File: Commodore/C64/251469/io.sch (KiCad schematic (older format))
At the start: 25 parts, among them CN4 Serial Bus, CN8 Control Port 2, CN9 Control Port 1, U1 6526, U2 6526, U27 74LS08, U28 4066, U8 7406

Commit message: refac: extracted serial bus to separate sheet
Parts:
- removed CN4: Serial Bus, symbol Connector:DIN-6
- added unit 1 of RP3
- added unit 2 of RP3
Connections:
- net labels removed: ATN, CLK, DATA, SRQ, ~EXTRST
- wire segments 194 -> 201
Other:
- note added: "CASS RD\nSRQ IN"
- note removed: "CASS RD"
- moved on the sheet: CR100, CR101, CR102, CR103
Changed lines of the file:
@@
 $Descr A4 11693 8268
 encoding utf-8
-Sheet 8 10
-Title "Commodore 64 - I/O section (schematic #251469)"
+Sheet 8 11
+Title "Commodore 64 - I/O Section (schematic #251469)"
 Date "2019-07-15"
 Rev "0.1"
@@
 Wire Wire Line
 	2700 4150 2950 4150
-Text HLabel 2700 7150 3    50   Output ~ 0
+Text HLabel 2700 7400 3    50   Output ~ 0
 ~IRQ
-Text HLabel 5600 7150 3    50   Output ~ 0
+Text HLabel 5600 7400 3    50   Output ~ 0
 ~NMI
-$Comp
-L Connector:DIN-6 CN4
-U 1 1 5D647908
-P 9500 3950
-F 0 "CN4" H 8600 4350 50  0000 C CNN
-F 1 "Serial Bus" H 8750 4250 50  0000 C CNN
-F 2 "" H 9500 3950 50  0001 C CNN
-F 3 "http://www.mouser.com/ds/2/18/40_c091_abd_e-75918.pdf" H 9500 3950 50  0001 C CNN
-	1    9500 3950
-	-1   0    0    -1
-$EndComp
-Wire Wire Line
-	10000 3900 10000 3850
-Text HLabel 9650 4300 2    50   Input ~ 0
-~EXTRST
-$Comp
-L power:GND #PWR?
-U 1 1 5D64C58B
-P 10000 3900
-F 0 "#PWR?" H 10000 3650 50  0001 C CNN
-F 1 "GND" H 10005 3727 50  0000 C CNN
-F 2 "" H 10000 3900 50  0001 C CNN
-F 3 "" H 10000 3900 50  0001 C CNN
-	1    10000 3900
-	-1   0    0    -1
-$EndComp
-Wire Wire Line
-	9500 4250 9500 4300
-Wire Wire Line
-	9500 4300 9650 4300
-Wire Wire Line
-	9200 4050 7850 4050
-Wire Wire Line
-	9200 3850 7850 3850
-Text Label 9200 4050 2    50   ~ 0
-DATA
-Text Label 9200 3850 2    50   ~ 0
-CLK
-Wire Wire Line
-	9500 3650 7850 3650
-Wire Wire Line
-	9800 3850 10000 3850
-Text Label 9500 3650 2    50   ~ 0
-ATN
-Wire Wire Line
-	9800 4050 9850 4050
-Wire Wire Line
-	9850 4050 9850 3550
-Wire Wire Line
-	9850 3550 7850 3550
-Text Label 9850 3550 2    50   ~ 0
-SRQ
-$Comp
-L Device:D CR100
-U 1 1 5D6E038A
-P -3300 4150
-F 0 "CR100" H -3300 4366 50  0000 C CNN
-F 1 "1N4148" H -3300 4275 50  0000 C CNN
-F 2 "" H -3300 4150 50  0001 C CNN
-F 3 "~" H -3300 4150 50  0001 C CNN
-	1    -3300 4150
-	1    0    0    -1
-$EndComp
 $Comp
 L Device:D CR101
 U 1 1 5D6E1332
-P -3300 4500
-F 0 "CR101" H -3300 4716 50  0000 C CNN
-F 1 "1N4148" H -3300 4625 50  0000 C CNN
-F 2 "" H -3300 4500 50  0001 C CNN
-F 3 "~" H -3300 4500 50  0001 C CNN
-	1    -3300 4500
-	1    0    0    -1
-$EndComp
-$Comp
-L Device:D CR102
-U 1 1 5D6E3186
-P -2750 4150
-F 0 "CR102" H -2750 4366 50  0000 C CNN
-F 1 "1N4148" H -2750 4275 50  0000 C CNN
-F 2 "" H -2750 4150 50  0001 C CNN
-F 3 "~" H -2750 4150 50  0001 C CNN
-	1    -2750 4150
-	1    0    0    -1
+P 8150 4450
+F 0 "CR101" H 8150 4666 50  0000 C CNN
+F 1 "1N4148" H 8150 4575 50  0000 C CNN
+F 2 "" H 8150 4450 50  0001 C CNN
+F 3 "~" H 8150 4450 50  0001 C CNN
+	1    8150 4450
+	0    1    1    0
 $EndComp
 $Comp
 L Device:D CR103
 U 1 1 5D6E318C
-P -2750 4500
-F 0 "CR103" H -2750 4716 50  0000 C CNN
-F 1 "1N4148" H -2750 4625 50  0000 C CNN
-F 2 "" H -2750 4500 50  0001 C CNN
-F 3 "~" H -2750 4500 50  0001 C CNN
-	1    -2750 4500
-	1    0    0    -1
+P 7800 4450
+F 0 "CR103" H 7800 4666 50  0000 C CNN
+F 1 "1N4148" H 7800 4575 50  0000 C CNN
+F 2 "" H 7800 4450 50  0001 C CNN
+F 3 "~" H 7800 4450 50  0001 C CNN
+	1    7800 4450
+	0    1    1    0
 $EndComp
 $Comp
@@
 $EndComp
 Text Notes 1550 5350 0    50   ~ 0
-CASS RD
+CASS RD\nSRQ IN
 Text Notes 5650 3450 0    50   ~ 0
 ~VA14
@@
 COL[0..7]
 Wire Wire Line
-	2700 5350 2700 7150
+	2700 5350 2700 7400
 Wire Wire Line
 	5600 5350 5600 6400
@@
 Wire Wire Line
 	4500 6400 5600 6400
-Connection ~ 5600 6400
-Wire Wire Line
-	5600 6400 5600 7150
+Wire Wire Line
+	5600 6400 5600 7250
 Wire Wire Line
 	6500 5850 6500 6200
@@
 	7150 3500 7600 3500
 Wire Wire Line
-	7300 3850 7600 3850
-Wire Wire Line
 	7050 4200 7450 4200
 Wire Wire Line
 	7450 3450 7450 4200
 Connection ~ 7450 4200
-Wire Wire Line
-	7450 4200 7600 4200
 Wire Wire Line
 	7150 3150 7150 3100
@@
 Wire Wire Line
 	7450 4600 7450 4200
+Wire Wire Line
+	7600 3500 7600 2700
+Wire Wire Line
+	7450 4200 8150 4200
+Wire Wire Line
+	8150 4200 8150 4300
+Connection ~ 7800 3850
+Wire Wire Line
+	7800 3850 7800 4300
+Wire Wire Line
+	7300 3850 7800 3850
+Connection ~ 8150 4200
+Wire Wire Line
+	7800 3850 7800 3450
+$Comp
+L Device:D CR102
+U 1 1 5D6E3186
+P 7800 3300
+F 0 "CR102" H 7800 3200 50  0000 C CNN
+F 1 "1N4148" H 7800 3425 50  0000 C CNN
+F 2 "" H 7800 3300 50  0001 C CNN
+F 3 "~" H 7800 3300 50  0001 C CNN
+	1    7800 3300
+	0    1    1    0
+$EndComp
+Wire Wire Line
+	7800 3150 7800 3100
+Wire Wire Line
+	7850 3100 8150 3100
+Connection ~ 7850 3100
+Wire Wire Line
+	7850 3050 7850 3100
+$Comp
+L power:+5V #PWR?
+U 1 1 5DD390BE
+P 7850 3050
+AR Path="/5DD390BE" Ref="#PWR?"  Part="1"
+AR Path="/5D28EBAC/5DD390BE" Ref="#PWR?"  Part="1"
+AR Path="/5D4AE438/5DD390BE" Ref="#PWR?"  Part="1"
+AR Path="/5D943305/5DD390BE" Ref="#PWR?"  Part="1"
+AR Path="/5D943305/5D47A471/5DD390BE" Ref="#PWR?"  Part="1"
+F 0 "#PWR?" H 7850 2900 50  0001 C CNN
+F 1 "+5V" H 7750 3200 50  0000 L CNN
+F 2 "" H 7850 3050 50  0001 C CNN
+F 3 "" H 7850 3050 50  0001 C CNN
+	1    7850 3050
+	1    0    0    -1
+$EndComp
+Wire Wire Line
+	8150 3100 8150 3150
+Wire Wire Line
+	7800 3100 7850 3100
+Wire Wire Line
+	8150 4200 8150 3450
+$Comp
+L Device:D CR100
+U 1 1 5D6E038A
+P 8150 3300
+F 0 "CR100" H 8150 3200 50  0000 C CNN
+F 1 "1N4148" H 8150 3425 50  0000 C CNN
+F 2 "" H 8150 3300 50  0001 C CNN
+F 3 "~" H 8150 3300 50  0001 C CNN
+	1    8150 3300
+	0    1    1    0
+$EndComp
+Wire Wire Line
+	7800 3850 8550 3850
+Wire Wire Line
+	8150 4200 8550 4200
+Wire Wire Line
+	7600 3500 8550 3500
+Connection ~ 7600 3500
+$Sheet
+S 9300 5050 750  350
+U 5DDE0343
+F0 "Serial Bus" 50
+F1 "serialbus.sch" 50
+$EndSheet
+$Comp
+L C64B:R_Network07_Split RP3
+U 1 1 5DE0B263
+P 4600 5100
+AR Path="/5D943305/5DE0B263" Ref="RP3"  Part="1"
+AR Path="/5D943305/5D47A471/5DE0B263" Ref="RP?"  Part="7"
+F 0 "RP3" V 4700 5000 50  0000 L CNN
+F 1 "3k3" V 4600 5050 25  0000 L CNN
+F 2 "" H 4700 5100 50  0001 C CNN
+F 3 "" H 4700 5100 50  0001 C CNN
+	1    4600 5100
+	1    0    0    -1
+$EndComp
+Connection ~ 4600 5350
+Wire Wire Line
+	4600 5350 4600 5300
+$Comp
+L power:+5V #PWR?
+U 1 1 5DE2E5EA
+P 4600 4850
+AR Path="/5DE2E5EA" Ref="#PWR?"  Part="1"
+AR Path="/5D28EBAC/5DE2E5EA" Ref="#PWR?"  Part="1"
+AR Path="/5D4AE438/5DE2E5EA" Ref="#PWR?"  Part="1"
+AR Path="/5D943305/5DE2E5EA" Ref="#PWR?"  Part="1"
+AR Path="/5D943305/5D47A471/5DE2E5EA" Ref="#PWR?"  Part="1"
+F 0 "#PWR?" H 4600 4700 50  0001 C CNN
+F 1 "+5V" H 4500 5000 50  0000 L CNN
+F 2 "" H 4600 4850 50  0001 C CNN
+F 3 "" H 4600 4850 50  0001 C CNN
+	1    4600 4850
+	1    0    0    -1
+$EndComp
+Wire Wire Line
+	4600 4850 4600 4900
+$Comp
+L C64B:R_Network07_Split RP3
+U 2 1 5DE3ABE8
+P 5800 7250
+AR Path="/5D943305/5DE3ABE8" Ref="RP3"  Part="2"
+AR Path="/5D943305/5D47A471/5DE3ABE8" Ref="RP?"  Part="7"
+F 0 "RP3" V 5900 7150 50  0000 L CNN
+F 1 "3k3" V 5800 7200 25  0000 L CNN
+F 2 "" H 5900 7250 50  0001 C CNN
+F 3 "" H 5900 7250 50  0001 C CNN
+	2    5800 7250
+	0    1    1    0
+$EndComp
+Connection ~ 5600 7250
+Wire Wire Line
+	5600 7250 5600 7400
+$Comp
+L power:+5V #PWR?
+U 1 1 5DE69A12
+P 6000 7200
+AR Path="/5DE69A12" Ref="#PWR?"  Part="1"
+AR Path="/5D28EBAC/5DE69A12" Ref="#PWR?"  Part="1"
+AR Path="/5D4AE438/5DE69A12" Ref="#PWR?"  Part="1"
+AR Path="/5D943305/5DE69A12" Ref="#PWR?"  Part="1"
+AR Path="/5D943305/5D47A471/5DE69A12" Ref="#PWR?"  Part="1"
+F 0 "#PWR?" H 6000 7050 50  0001 C CNN
+F 1 "+5V" H 5900 7350 50  0000 L CNN
+F 2 "" H 6000 7200 50  0001 C CNN
+F 3 "" H 6000 7200 50  0001 C CNN
+	1    6000 7200
+	1    0    0    -1
+$EndComp
+Connection ~ 5600 6400
+Wire Wire Line
+	6000 7250 6000 7200
 Wire Bus Line
 	4500 1100 4500 2750

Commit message: wip
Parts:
- added unit 3 of RP3
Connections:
- net labels added: ~EXTRST
- wire segments 201 -> 225
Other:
- moved on the sheet: C200, CR1, CR104, CR105, R100, R37, R5, U27C

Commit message: Using extracted R_Network07_Split from new Resistor_Pack library instead of embedding it in C64B library
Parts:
- removed RP3: 3k3, symbol C64B:R_Network07_Split
- added RP3: 3k3, symbol Resistor_Pack:R_Network07_Split
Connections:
- wire segments 225 -> 227
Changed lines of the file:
@@
 	4450 4250 4500 4250
 Wire Wire Line
-	4500 4250 4500 6500
-Wire Wire Line
 	4500 6500 5600 6500
-Wire Wire Line
-	5600 6500 5600 7350
 Wire Wire Line
 	7100 5850 7100 6200
@@
 	1    0    0    -1
 $EndComp
-$Comp
-L C64B:R_Network07_Split RP3
-U 4 1 5D94F7D8
-P 3950 6050
-AR Path="/5D943305/5D94F7D8" Ref="RP3"  Part="4"
-AR Path="/5D943305/5D47A471/5D94F7D8" Ref="RP?"  Part="4"
-F 0 "RP3" V 3950 6375 50  0000 L CNN
-F 1 "3k3" V 3950 6000 25  0000 L CNN
-F 2 "" H 4050 6050 50  0001 C CNN
-F 3 "" H 4050 6050 50  0001 C CNN
-	4    3950 6050
-	0    1    1    0
-$EndComp
-$Comp
-L C64B:R_Network07_Split RP3
-U 5 1 5D94F7DE
-P 3950 5950
-AR Path="/5D943305/5D94F7DE" Ref="RP3"  Part="5"
-AR Path="/5D943305/5D47A471/5D94F7DE" Ref="RP?"  Part="5"
-F 0 "RP3" V 3950 6275 50  0000 L CNN
-F 1 "3k3" V 3950 5900 25  0000 L CNN
-F 2 "" H 4050 5950 50  0001 C CNN
-F 3 "" H 4050 5950 50  0001 C CNN
-	5    3950 5950
-	0    1    1    0
-$EndComp
-$Comp
-L C64B:R_Network07_Split RP3
-U 6 1 5D94F7E4
-P 3950 5850
-AR Path="/5D943305/5D94F7E4" Ref="RP3"  Part="6"
-AR Path="/5D943305/5D47A471/5D94F7E4" Ref="RP?"  Part="6"
-F 0 "RP3" V 3950 6175 50  0000 L CNN
-F 1 "3k3" V 3950 5800 25  0000 L CNN
-F 2 "" H 4050 5850 50  0001 C CNN
-F 3 "" H 4050 5850 50  0001 C CNN
-	6    3950 5850
-	0    1    1    0
-$EndComp
 Wire Wire Line
 	3750 5750 3550 5750
@@
 Wire Wire Line
 	3750 6050 3250 6050
-$Comp
-L C64B:R_Network07_Split RP3
-U 7 1 5D94F7EA
-P 3950 5750
-AR Path="/5D943305/5D94F7EA" Ref="RP3"  Part="7"
-AR Path="/5D943305/5D47A471/5D94F7EA" Ref="RP?"  Part="7"
-F 0 "RP3" V 3950 6075 50  0000 L CNN
-F 1 "3k3" V 3950 5700 25  0000 L CNN
-F 2 "" H 4050 5750 50  0001 C CNN
-F 3 "" H 4050 5750 50  0001 C CNN
-	7    3950 5750
-	0    1    1    0
-$EndComp
 Connection ~ 3250 6050
 Connection ~ 3350 5950
@@
 	7450 3100 7300 3100
 Wire Wire Line
-	4150 5750 4200 5750
-Wire Wire Line
-	4200 5750 4200 5850
-Wire Wire Line
-	4200 5850 4150 5850
-Wire Wire Line
-	4200 5850 4200 5950
-Wire Wire Line
-	4200 5950 4150 5950
-Connection ~ 4200 5850
-Wire Wire Line
-	4200 5950 4200 6050
-Wire Wire Line
-	4200 6050 4150 6050
-Connection ~ 4200 5950
+	4050 5750 4100 5750
+Wire Wire Line
+	4100 5750 4100 5850
+Wire Wire Line
+	4100 5850 4050 5850
+Wire Wire Line
+	4100 5850 4100 5950
+Wire Wire Line
+	4100 5950 4050 5950
+Connection ~ 4100 5850
+Wire Wire Line
+	4100 5950 4100 6050
+Wire Wire Line
+	4100 6050 4050 6050
+Connection ~ 4100 5950
 $Comp
 L power:+5V #PWR?
 U 1 1 5D94F7F0
-P 4200 5650
+P 4100 5650
 AR Path="/5D94F7F0" Ref="#PWR?"  Part="1"
 AR Path="/5D28EBAC/5D94F7F0" Ref="#PWR?"  Part="1"
@@
 AR Path="/5D943305/5D94F7F0" Ref="#PWR?"  Part="1"
 AR Path="/5D943305/5D47A471/5D94F7F0" Ref="#PWR?"  Part="1"
-F 0 "#PWR?" H 4200 5500 50  0001 C CNN
-F 1 "+5V" H 4100 5800 50  0000 L CNN
-F 2 "" H 4200 5650 50  0001 C CNN
-F 3 "" H 4200 5650 50  0001 C CNN
-	1    4200 5650
-	1    0    0    -1
-$EndComp
-Wire Wire Line
-	4200 5650 4200 5750
-Connection ~ 4200 5750
+F 0 "#PWR?" H 4100 5500 50  0001 C CNN
+F 1 "+5V" H 4000 5800 50  0000 L CNN
+F 2 "" H 4100 5650 50  0001 C CNN
+F 3 "" H 4100 5650 50  0001 C CNN
+	1    4100 5650
+	1    0    0    -1
+$EndComp
+Wire Wire Line
+	4100 5650 4100 5750
+Connection ~ 4100 5750
 Wire Wire Line
 	5600 4050 6300 4050
@@
 F6 "~SRQ" O R 9900 3450 50
 $EndSheet
-$Comp
-L C64B:R_Network07_Split RP3
-U 1 1 5DE0B263
-P 4600 5100
-AR Path="/5D943305/5DE0B263" Ref="RP3"  Part="1"
-AR Path="/5D943305/5D47A471/5DE0B263" Ref="RP?"  Part="7"
-F 0 "RP3" V 4700 5000 50  0000 L CNN
-F 1 "3k3" V 4600 5050 25  0000 L CNN
-F 2 "" H 4700 5100 50  0001 C CNN
-F 3 "" H 4700 5100 50  0001 C CNN
-	1    4600 5100
-	1    0    0    -1
-$EndComp
 Connection ~ 4600 5350
 Wire Wire Line
 	4600 5350 4600 5300
-$Comp
-L power:+5V #PWR?
-U 1 1 5DE2E5EA
-P 4600 4850
-AR Path="/5DE2E5EA" Ref="#PWR?"  Part="1"
-AR Path="/5D28EBAC/5DE2E5EA" Ref="#PWR?"  Part="1"
-AR Path="/5D4AE438/5DE2E5EA" Ref="#PWR?"  Part="1"
-AR Path="/5D943305/5DE2E5EA" Ref="#PWR?"  Part="1"
-AR Path="/5D943305/5D47A471/5DE2E5EA" Ref="#PWR?"  Part="1"
-F 0 "#PWR?" H 4600 4700 50  0001 C CNN
-F 1 "+5V" H 4500 5000 50  0000 L CNN
-F 2 "" H 4600 4850 50  0001 C CNN
-F 3 "" H 4600 4850 50  0001 C CNN
-	1    4600 4850
-	1    0    0    -1
-$EndComp
-Wire Wire Line
-	4600 4850 4600 4900
-$Comp
-L C64B:R_Network07_Split RP3
-U 2 1 5DE3ABE8
-P 5800 7350
-AR Path="/5D943305/5DE3ABE8" Ref="RP3"  Part="2"
-AR Path="/5D943305/5D47A471/5DE3ABE8" Ref="RP?"  Part="7"
-F 0 "RP3" V 5900 7250 50  0000 L CNN
-F 1 "3k3" V 5800 7300 25  0000 L CNN
-F 2 "" H 5900 7350 50  0001 C CNN
-F 3 "" H 5900 7350 50  0001 C CNN
-	2    5800 7350
-	0    1    1    0
-$EndComp
-Connection ~ 5600 7350
-Wire Wire Line
-	5600 7350 5600 7500
 $Comp
 L power:+5V #PWR?
 U 1 1 5DE69A12
-P 6000 7300
+P 6000 7350
 AR Path="/5DE69A12" Ref="#PWR?"  Part="1"
 AR Path="/5D28EBAC/5DE69A12" Ref="#PWR?"  Part="1"
@@
 AR Path="/5D943305/5DE69A12" Ref="#PWR?"  Part="1"
 AR Path="/5D943305/5D47A471/5DE69A12" Ref="#PWR?"  Part="1"
-F 0 "#PWR?" H 6000 7150 50  0001 C CNN
-F 1 "+5V" H 5900 7450 50  0000 L CNN
-F 2 "" H 6000 7300 50  0001 C CNN
-F 3 "" H 6000 7300 50  0001 C CNN
-	1    6000 7300
+F 0 "#PWR?" H 6000 7200 50  0001 C CNN
+F 1 "+5V" H 5900 7500 50  0000 L CNN
+F 2 "" H 6000 7350 50  0001 C CNN
+F 3 "" H 6000 7350 50  0001 C CNN
+	1    6000 7350
 	1    0    0    -1
 $EndComp
 Connection ~ 5600 6500
 Wire Wire Line
-	6000 7350 6000 7300
+	6000 7400 6000 7350
 Wire Wire Line
 	1900 5350 1700 5350
@@
 CASS RD\nSRQ IN
 $Comp
-L C64B:R_Network07_Split RP3
-U 3 1 5DF27A37
-P 1700 5100
-AR Path="/5D943305/5DF27A37" Ref="RP3"  Part="3"
-AR Path="/5D943305/5D47A471/5DF27A37" Ref="RP?"  Part="7"
-F 0 "RP3" V 1800 5000 50  0000 L CNN
-F 1 "3k3" V 1700 5050 25  0000 L CNN
-F 2 "" H 1800 5100 50  0001 C CNN
-F 3 "" H 1800 5100 50  0001 C CNN
-	3    1700 5100
-	1    0    0    -1
-$EndComp
-$Comp
 L power:+5V #PWR?
 U 1 1 5DF27A3D
-P 1700 4850
+P 1700 4950
 AR Path="/5DF27A3D" Ref="#PWR?"  Part="1"
 AR Path="/5D28EBAC/5DF27A3D" Ref="#PWR?"  Part="1"
@@
 AR Path="/5D943305/5DF27A3D" Ref="#PWR?"  Part="1"
 AR Path="/5D943305/5D47A471/5DF27A3D" Ref="#PWR?"  Part="1"
-F 0 "#PWR?" H 1700 4700 50  0001 C CNN
-F 1 "+5V" H 1600 5000 50  0000 L CNN
-F 2 "" H 1700 4850 50  0001 C CNN
-F 3 "" H 1700 4850 50  0001 C CNN
-	1    1700 4850
-	1    0    0    -1
-$EndComp
-Wire Wire Line
-	1700 4850 1700 4900
+F 0 "#PWR?" H 1700 4800 50  0001 C CNN
+F 1 "+5V" H 1600 5100 50  0000 L CNN
+F 2 "" H 1700 4950 50  0001 C CNN
+F 3 "" H 1700 4950 50  0001 C CNN
+	1    1700 4950
+	1    0    0    -1
+$EndComp
+Wire Wire Line
+	1700 4950 1700 5000
 Wire Wire Line
 	1700 5350 1700 5300
@@
 Wire Wire Line
 	10000 3450 9900 3450
+Wire Wire Line
+	4600 4950 4600 5000
+$Comp
+L power:+5V #PWR?
+U 1 1 5DE2E5EA
+P 4600 4950
+AR Path="/5DE2E5EA" Ref="#PWR?"  Part="1"
+AR Path="/5D28EBAC/5DE2E5EA" Ref="#PWR?"  Part="1"
+AR Path="/5D4AE438/5DE2E5EA" Ref="#PWR?"  Part="1"
+AR Path="/5D943305/5DE2E5EA" Ref="#PWR?"  Part="1"
+AR Path="/5D943305/5D47A471/5DE2E5EA" Ref="#PWR?"  Part="1"
+F 0 "#PWR?" H 4600 4800 50  0001 C CNN
+F 1 "+5V" H 4500 5100 50  0000 L CNN
+F 2 "" H 4600 4950 50  0001 C CNN
+F 3 "" H 4600 4950 50  0001 C CNN
+	1    4600 4950
+	1    0    0    -1
+$EndComp
+Wire Wire Line
+	4500 4250 4500 6500
+$Comp
+L Resistor_Pack:R_Network07_Split RP3
+U 1 1 5D359677
+P 4600 5150
+F 0 "RP3" V 4500 5150 50  0000 C CNN
+F 1 "3k3" V 4600 5150 30  0000 C CNN
+F 2 "" H 4600 5150 50  0001 C CNN
+F 3 "http://www.vishay.com/docs/31509/csc.pdf" H 4600 5150 50  0001 C CNN
+	1    4600 5150
+	-1   0    0    1
+$EndComp
+$Comp
+L Resistor_Pack:R_Network07_Split RP3
+U 3 1 5D39D797
+P 1700 5150
+F 0 "RP3" V 1600 5150 50  0000 C CNN
+F 1 "3k3" V 1700 5150 30  0000 C CNN
+F 2 "" H 1700 5150 50  0001 C CNN
+F 3 "http://www.vishay.com/docs/31509/csc.pdf" H 1700 5150 50  0001 C CNN
+	3    1700 5150
+	-1   0    0    -1
+$EndComp
+$Comp
+L Resistor_Pack:R_Network07_Split RP3
+U 2 1 5D3C33C5
+P 5800 7400
+F 0 "RP3" V 5700 7400 50  0000 C CNN
+F 1 "3k3" V 5800 7400 30  0000 C CNN
+F 2 "" H 5800 7400 50  0001 C CNN
+F 3 "http://www.vishay.com/docs/31509/csc.pdf" H 5800 7400 50  0001 C CNN
+	2    5800 7400
+	0    1    1    0
+$EndComp
+Wire Wire Line
+	5600 6500 5600 7400
+Wire Wire Line
+	5650 7400 5600 7400
+Connection ~ 5600 7400
+Wire Wire Line
+	5600 7400 5600 7500
+Wire Wire Line
+	5950 7400 6000 7400
+$Comp
+L Resistor_Pack:R_Network07_Split RP3
+U 7 1 5D3FF4BF
+P 3900 5750
+F 0 "RP3" V 3900 6100 50  0000 C CNN
+F 1 "3k3" V 3900 5750 30  0000 C CNN
+F 2 "" H 3900 5750 50  0001 C CNN
+F 3 "http://www.vishay.com/docs/31509/csc.pdf" H 3900 5750 50  0001 C CNN
+	7    3900 5750
+	0    1    1    0
+$EndComp
+$Comp
+L Resistor_Pack:R_Network07_Split RP3
+U 6 1 5D401D35
+P 3900 5850
+F 0 "RP3" V 3900 6200 50  0000 C CNN
+F 1 "3k3" V 3900 5850 30  0000 C CNN
+F 2 "" H 3900 5850 50  0001 C CNN
+F 3 "http://www.vishay.com/docs/31509/csc.pdf" H 3900 5850 50  0001 C CNN
+	6    3900 5850
+	0    1    1    0
+$EndComp
+$Comp
+L Resistor_Pack:R_Network07_Split RP3
+U 5 1 5D4039CF
+P 3900 5950
+F 0 "RP3" V 3900 6300 50  0000 C CNN
+F 1 "3k3" V 3900 5950 30  0000 C CNN
+F 2 "" H 3900 5950 50  0001 C CNN
+F 3 "http://www.vishay.com/docs/31509/csc.pdf" H 3900 5950 50  0001 C CNN
+	5    3900 5950
+	0    1    1    0
+$EndComp
+$Comp
+L Resistor_Pack:R_Network07_Split RP3
+U 4 1 5D404120
+P 3900 6050
+F 0 "RP3" V 3900 6400 50  0000 C CNN
+F 1 "3k3" V 3900 6050 30  0000 C CNN
+F 2 "" H 3900 6050 50  0001 C CNN
+F 3 "http://www.vishay.com/docs/31509/csc.pdf" H 3900 6050 50  0001 C CNN
+	4    3900 6050
+	0    1    1    0
+$EndComp
 Wire Bus Line
 	4500 1100 4500 2750

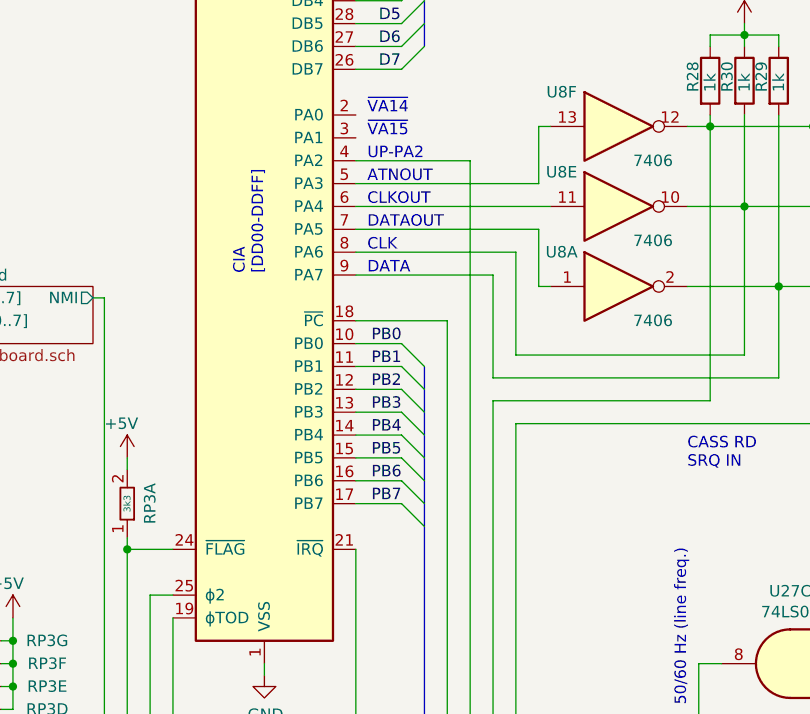
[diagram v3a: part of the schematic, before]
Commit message: Net labels for serial bus CIA lines
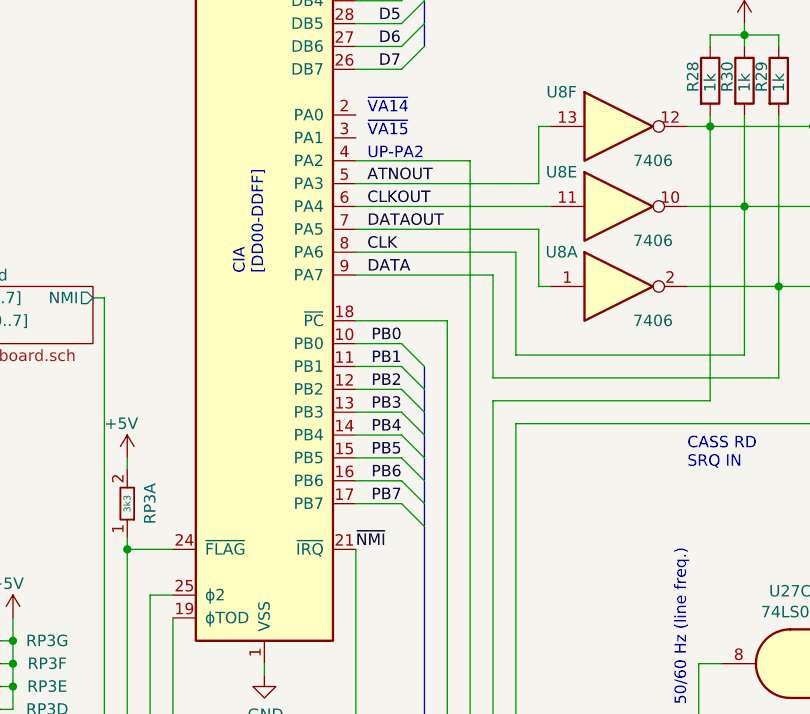
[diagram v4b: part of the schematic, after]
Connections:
- net DATAOUT: now reaches U2.7 (PA5), U8.1
- net CLKOUT: now reaches U2.6 (PA4), U8.11
- net ATNOUT: now reaches U2.5 (PA3), U8.13
- net Serial Bus/CLK renamed CLK
- net Serial Bus/DATA renamed DATA
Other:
- note removed: "ATNOUT"
- note removed: "CLK"
- note removed: "CLKOUT"
- note removed: "DATA"
- note removed: "DATAOUT"
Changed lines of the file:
@@
 Text Notes 5650 3650 0    50   ~ 0
 UP-PA2
-Text Notes 5650 3750 0    50   ~ 0
-ATNOUT
-Text Notes 5650 3850 0    50   ~ 0
-CLKOUT
-Text Notes 5650 3950 0    50   ~ 0
-DATAOUT
-Text Notes 5650 4050 0    50   ~ 0
-CLK
-Text Notes 5650 4150 0    50   ~ 0
-DATA
 $Comp
 L Connector:DB9_Male CN8
@@
 Wire Bus Line
 	3000 1000 3000 3150
+Text Label 5600 5350 0    50   ~ 0
+~NMI
+Text Label 5650 3750 0    50   ~ 0
+ATNOUT
+Text Label 5650 3850 0    50   ~ 0
+CLKOUT
+Text Label 5650 3950 0    50   ~ 0
+DATAOUT
+Text Label 5650 4050 0    50   ~ 0
+CLK
+Text Label 5650 4150 0    50   ~ 0
+DATA
 $EndSCHEMATC
